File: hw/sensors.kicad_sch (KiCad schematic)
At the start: 29 parts, among them J201 BNC, U401 OPA990, U402 INA210, U403 OPA990, U404 INA210

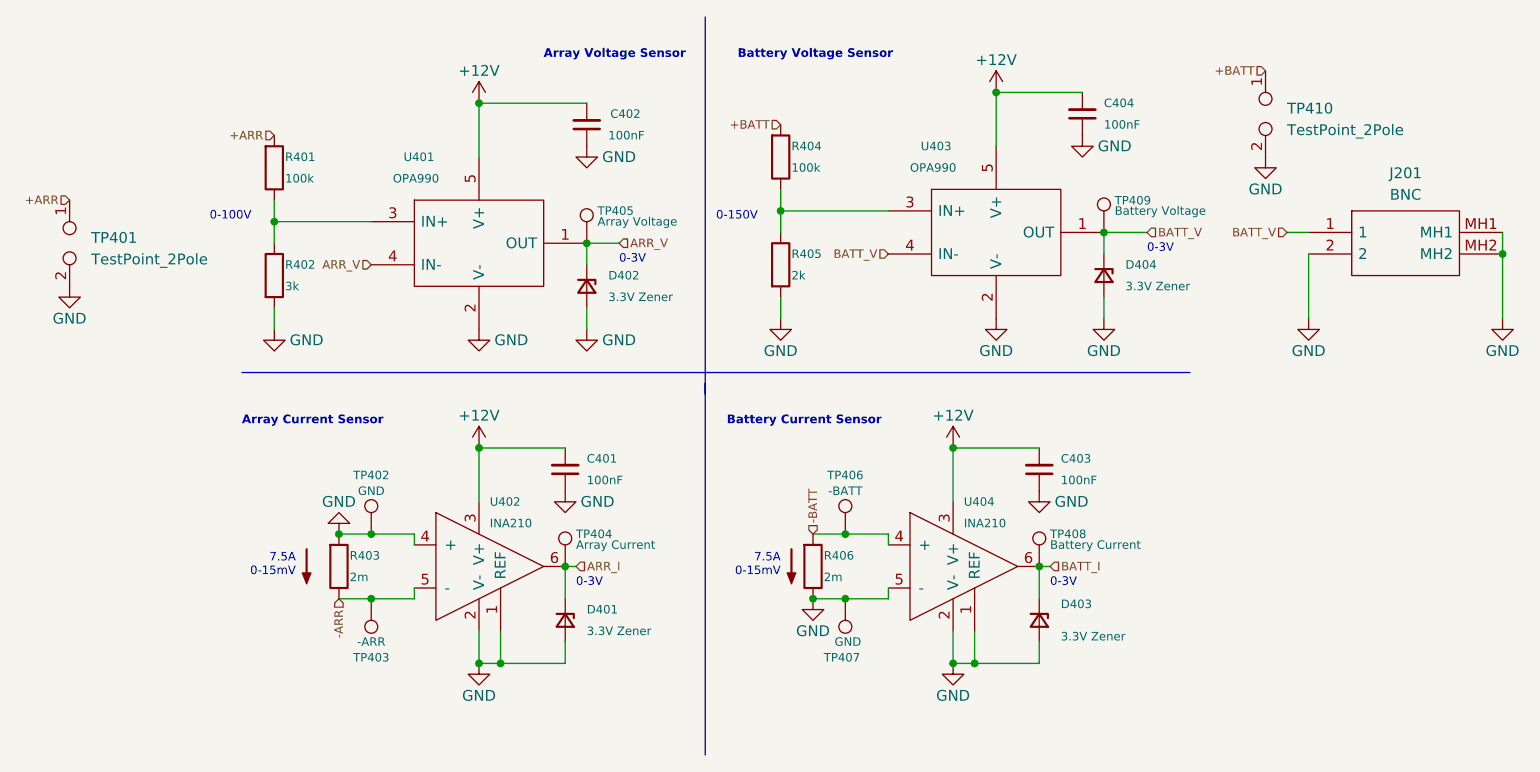
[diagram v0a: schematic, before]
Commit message: production files for v0.1.0. Change cap power calc to be based off i_rms of i_pkpk, not i_pk + r_l_a
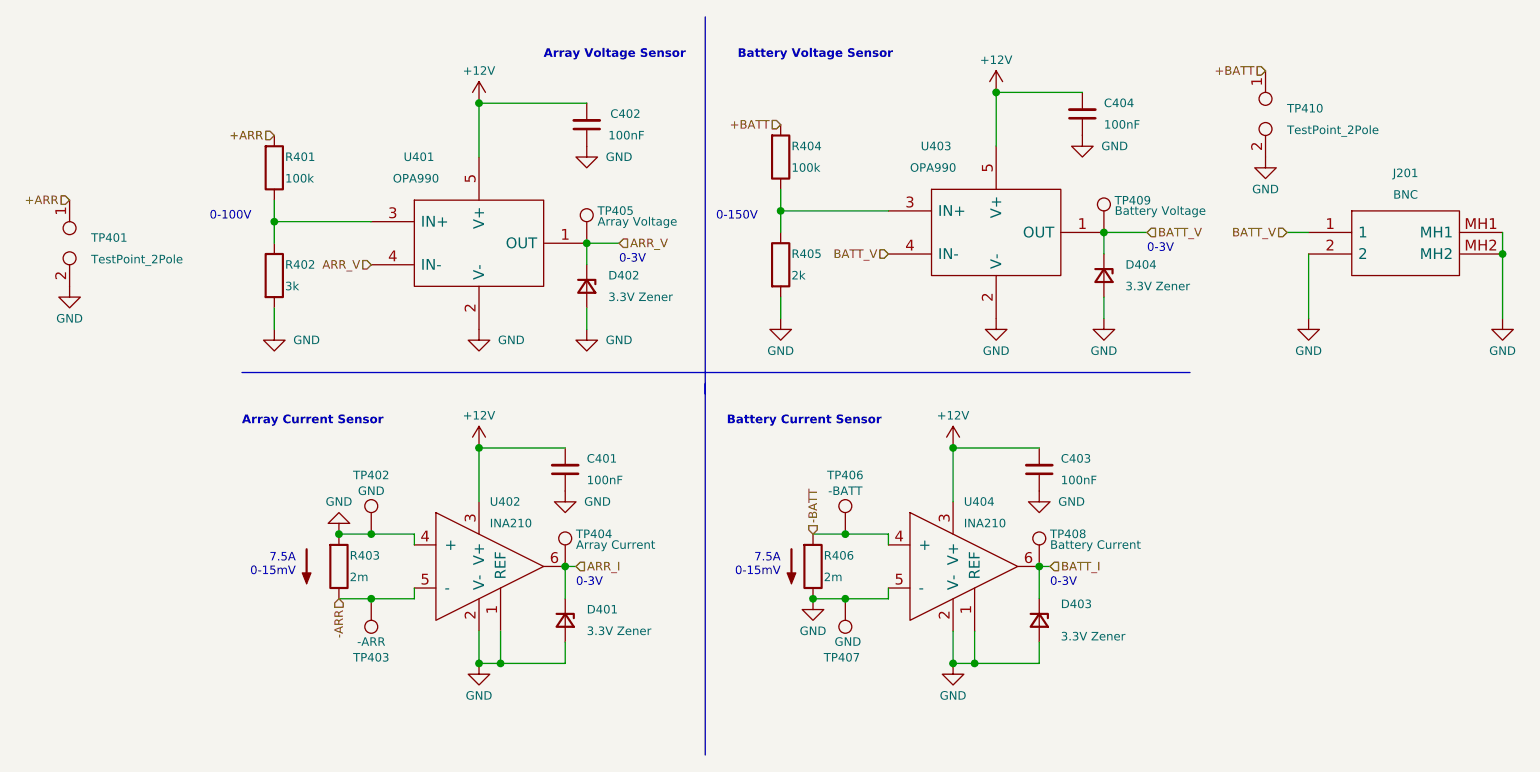
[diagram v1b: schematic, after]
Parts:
- C401, C402, C403, C404: LCSC Part # (none) -> C307331
- D401, D402, D403, D404: LCSC Part # (none) -> C8056
- R401, R404: LCSC Part # (none) -> C149504
- R402: LCSC Part # (none) -> C17661
- R405: LCSC Part # (none) -> C17604
- U402, U404: Distributor Texas Instruments -> Mouser

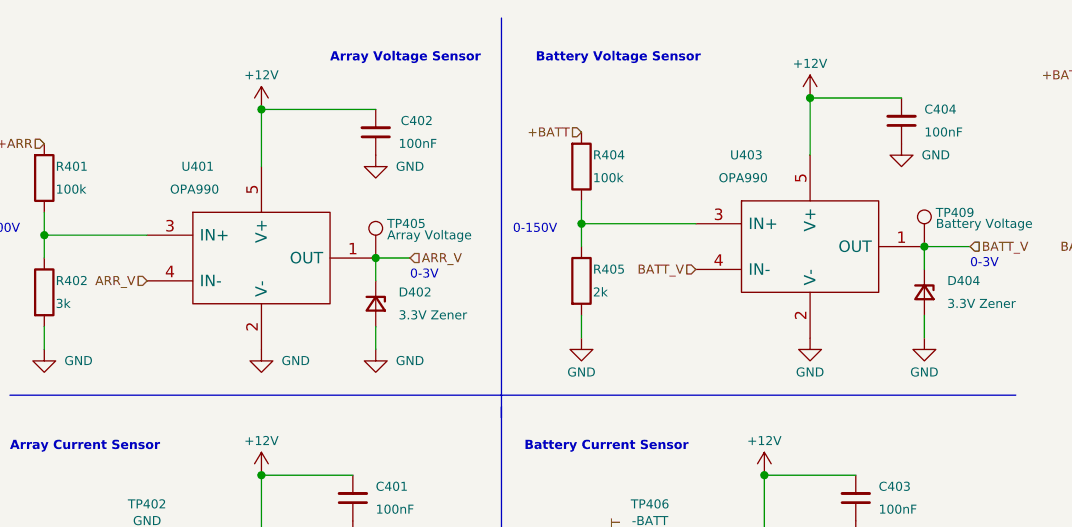
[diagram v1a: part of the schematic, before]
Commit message: fixes for v0.1.1rc
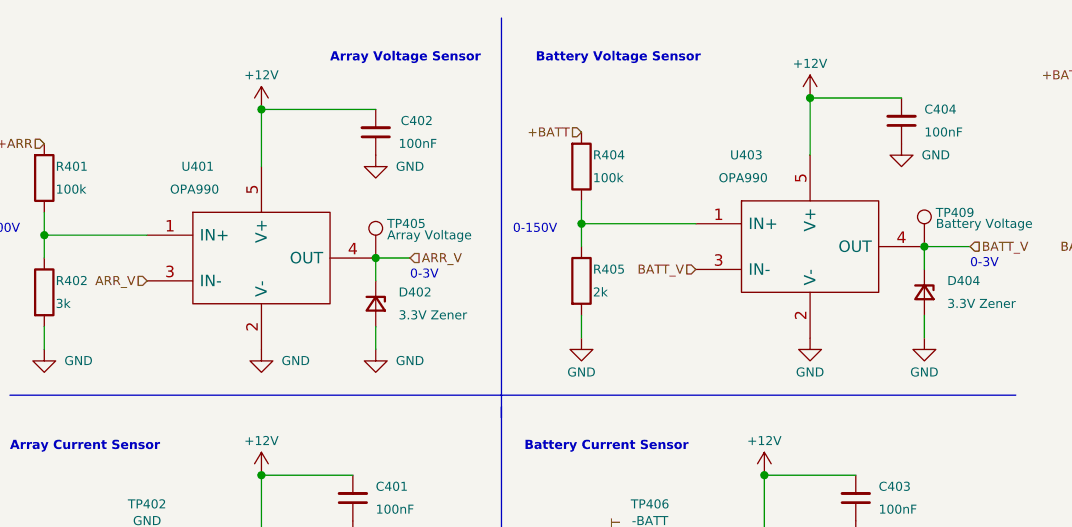
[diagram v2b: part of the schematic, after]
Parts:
- U401, U403: footprint mppt:SOT65P210X110-5N -> SOT65P210X110-5N; Height (none) -> 1.1; Manufacturer_Name (none) -> Texas Instruments; Manufacturer_Part_Number (none) -> OPA990IDCKR; Mouser Part Number (none) -> 595-OPA990IDCKR; Mouser Price/Stock (none) -> https://www.mouser.co.uk/ProductDetail/Texas-Instruments/OP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
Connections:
- net ARR_V: now also U401.3 (IN-); no longer U401.1 (OUT)
- net BATT_V: now also U403.3 (IN-); no longer U403.1 (OUT)
- net at R401.1, R402.1: now also U401.1 (IN+); no longer U401.3 (IN+)
- net at R404.1, R405.1: now also U403.1 (IN+); no longer U403.3 (IN+)
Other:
- company: (none) -> UT LHR Solar
- title: MPPT -> Sunscatter MPPT
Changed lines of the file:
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@@
   (paper "A4")
   (title_block
-    (title "MPPT")
-    (date "2023-01-30")
-    (rev "v0.0.0")
-    (comment 1 "Nishant Gupta")
+    (title "Sunscatter MPPT")
+    (date "2023-03-26")
+    (rev "v0.1.1")
+    (company "UT LHR Solar")
+    (comment 1 "Matthew Yu")
     (comment 2 "Jacob Pustilnik")
   )
@@
       (effects (font (size 1 1)) (justify left))
     )
-    (property "Footprint" "mppt:SOT65P210X110-5N" (at 190.5 71.12 0)
+    (property "Footprint" "SOT65P210X110-5N" (at 190.5 71.12 0)
       (effects (font (size 1.27 1.27)) (justify left) hide)
     )
@@
       (effects (font (size 1.27 1.27)) hide)
     )
-    (pin "1")
+    (property "Description" "Texas Instruments" (at 190.5 76.2 0)
+      (effects (font (size 1.27 1.27)) (justify left) hide)
+    )
+    (property "Height" "1.1" (at 190.5 78.74 0)
+      (effects (font (size 1.27 1.27)) (justify left) hide)
+    )
+    (property "Mouser Part Number" "595-OPA990IDCKR" (at 190.5 81.28 0)
+      (effects (font (size 1.27 1.27)) (justify left) hide)
+    )
+    (property "Mouser Price/Stock" "https://www.mouser.co.uk/ProductDetail/Texas-Instruments/OPA990IDCKR?qs=XeJtXLiO41TSF5QBGuARgQ%3D%3D" (at 190.5 83.82 0)
+      (effects (font (size 1.27 1.27)) (justify left) hide)
+    )
+    (property "Manufacturer_Name" "Texas Instruments" (at 190.5 86.36 0)
+      (effects (font (size 1.27 1.27)) (justify left) hide)
+    )
+    (property "Manufacturer_Part_Number" "OPA990IDCKR" (at 190.5 88.9 0)
+      (effects (font (size 1.27 1.27)) (justify left) hide)
+    )
     (pin "2")
+    (pin "5")
+    (pin "1")
     (pin "3")
     (pin "4")
-    (pin "5")
     (instances
       (project "mppt"
@@
       (effects (font (size 1 1)) (justify left))
     )
-    (property "Footprint" "mppt:SOT65P210X110-5N" (at 129.54 72.39 0)
+    (property "Footprint" "SOT65P210X110-5N" (at 129.54 72.39 0)
       (effects (font (size 1.27 1.27)) (justify left) hide)
     )
@@
       (effects (font (size 1.27 1.27)) hide)
     )
-    (pin "1")
+    (property "Description" "Texas Instruments" (at 129.54 77.47 0)
+      (effects (font (size 1.27 1.27)) (justify left) hide)
+    )
+    (property "Height" "1.1" (at 129.54 80.01 0)
+      (effects (font (size 1.27 1.27)) (justify left) hide)
+    )
+    (property "Mouser Part Number" "595-OPA990IDCKR" (at 129.54 82.55 0)
+      (effects (font (size 1.27 1.27)) (justify left) hide)
+    )
+    (property "Mouser Price/Stock" "https://www.mouser.co.uk/ProductDetail/Texas-Instruments/OPA990IDCKR?qs=XeJtXLiO41TSF5QBGuARgQ%3D%3D" (at 129.54 85.09 0)
+      (effects (font (size 1.27 1.27)) (justify left) hide)
+    )
+    (property "Manufacturer_Name" "Texas Instruments" (at 129.54 87.63 0)
+      (effects (font (size 1.27 1.27)) (justify left) hide)
+    )
+    (property "Manufacturer_Part_Number" "OPA990IDCKR" (at 129.54 90.17 0)
+      (effects (font (size 1.27 1.27)) (justify left) hide)
+    )
     (pin "2")
+    (pin "5")
+    (pin "1")
     (pin "3")
     (pin "4")
-    (pin "5")
-    (instances
-      (project "mppt"
+    (instances
+      (project "mppt"

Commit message: updated instructions for v0.2.0 - v0.5.0 development candidates.
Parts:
- C401, C402, C403, C404: Cost (none) -> 0.0068; JLC P/N C307331 -> (none)
- D401, D402, D403, D404: Cost (none) -> 0.0106; JLC P/N C8056 -> (none)
- J201: Cost (none) -> 2.39
- R401, R404: Cost (none) -> 0.0017; JLC P/N C149504 -> (none)
- R402: Cost (none) -> 0.0018; JLC P/N C17661 -> (none)
- R403, R406: Cost (none) -> 0.73
- R405: Cost (none) -> 0.0018; JLC P/N C17604 -> (none)
- TP402, TP407: Cost (none) -> 0.31
- TP403, TP404, TP406, TP408: Cost (none) -> 0.39
- TP405, TP409: Cost (none) -> 0.33
- U401, U403: Cost (none) -> 0.593; Distributor Mouser -> Texas Instruments; Height 1.1 -> (none); Manufacturer_Name Texas Instruments -> (none); Manufacturer_Part_Number OPA990IDCKR -> (none); Mouser Part Number 595-OPA990IDCKR -> (none); Mouser Price/Stock https://www.mouser.co.uk/ProductDetail/Texas-Instruments/OP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 -> (none); P/N 595-OPA990IDCKR -> OPA990IDCKR
- U402, U404: Cost (none) -> 0.813; Distributor Mouser -> Texas Instruments

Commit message: hw changes
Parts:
- J201: footprint mppt:CONBNC002 -> footprints:CONBNC002
- TP401, TP410: footprint mppt:SignalTP -> footprints:SignalTP
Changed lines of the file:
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@@
       (effects (font (size 1 1)) (justify left))
     )
-    (property "Footprint" "mppt:SignalTP" (at 72.39 77.47 0)
+    (property "Footprint" "footprints:SignalTP" (at 72.39 77.47 0)
       (effects (font (size 1.27 1.27)) hide)
     )
@@
       (effects (font (size 1 1)))
     )
-    (property "Footprint" "mppt:CONBNC002" (at 237.49 73.66 0)
+    (property "Footprint" "footprints:CONBNC002" (at 237.49 73.66 0)
       (effects (font (size 1.27 1.27)) (justify left) hide)
     )
@@
       (effects (font (size 1 1)) (justify left))
     )
-    (property "Footprint" "mppt:SignalTP" (at 213.36 62.23 0)
-      (effects (font (size 1.27 1.27)) hide)
-    )
+    (property "Footprint" "footprints:SignalTP" (at 213.36 62.23 0)
+      (effects (font (size 1.27 1.27)) hide)
+    )

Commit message: v0.2.0
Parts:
- removed J201: BNC, footprints:CONBNC002, symbol CONBNC002:CONBNC002
- removed TP401, TP410: TestPoint_2Pole, footprints:SignalTP, symbol Connector:TestPoint_2Pole
- removed U401, U403: OPA990, SOT65P210X110-5N, symbol OPA990IDCKR:OPA990IDCKR
- removed U402, U404: INA210, Package_TO_SOT_SMD:SOT-363_SC-70-6_Handsoldering, symbol MPPT:OP_AMP_INA21x
- added IC401, IC404: INA210CQDCKRQ1, footprints:ti_INA210CQDCKRQ1, symbol ti_INA210CQDCKRQ1:INA210CQDCKRQ1
- added IC402, IC403: OPA990IDCKR, footprints:ti_OPA990IDCKR, symbol ti_OPA990IDCKR:OPA990IDCKR
- added TP401: +ARR_TP, TestPoint:TestPoint_Pad_1.0x1.0mm, symbol Connector:TestPoint
- added TP410: GND_TP, TestPoint:TestPoint_Pad_1.0x1.0mm, symbol Connector:TestPoint
- added TP411: BATTV_TP, TestPoint:TestPoint_Pad_1.0x1.0mm, symbol Connector:TestPoint
- added TP412: BATTI_TP, TestPoint:TestPoint_Pad_1.0x1.0mm, symbol Connector:TestPoint
- D402, D403: value 3.3V Zener -> 3V3
- TP402: value GND -> GND_TP; footprint TestPoint:TestPoint_Keystone_5000-5004_Miniature -> TestPoint:TestPoint_Pad_1.0x1.0mm; Color Black -> (none); Cost 0.31 -> (none); Distributor Mouser -> (none); Manufacturer Keystone Electronics -> (none); P/N 534-5001 -> (none)
- TP403: value -ARR -> GND_TP; footprint TestPoint:TestPoint_Keystone_5000-5004_Miniature -> TestPoint:TestPoint_Pad_1.0x1.0mm; Color Brown -> (none); Cost 0.39 -> (none); Distributor Mouser -> (none); Manufacturer Keystone Electronics -> (none); P/N 534-5115 -> (none)
- TP404: value Array Current -> -ARR_TP; footprint TestPoint:TestPoint_Keystone_5000-5004_Miniature -> TestPoint:TestPoint_Pad_1.0x1.0mm; Color Blue -> (none); Cost 0.39 -> (none); Distributor Mouser -> (none); Manufacturer Keystone Electronics -> (none); P/N 534-5117 -> (none)
- TP405: value Array Voltage -> ARRI_TP; footprint TestPoint:TestPoint_Keystone_5000-5004_Miniature -> TestPoint:TestPoint_Pad_1.0x1.0mm; Color Green -> (none); Cost 0.33 -> (none); Distributor Mouser -> (none); Manufacturer Keystone Electronics -> (none); P/N 534-5116 -> (none)
- TP406: value -BATT -> ARRV_TP; footprint TestPoint:TestPoint_Keystone_5000-5004_Miniature -> TestPoint:TestPoint_Pad_1.0x1.0mm; Color Brown -> (none); Cost 0.39 -> (none); Distributor Mouser -> (none); Manufacturer Keystone Electronics -> (none); P/N 534-5115 -> (none)
- TP407: value GND -> +BATT_TP; footprint TestPoint:TestPoint_Keystone_5000-5004_Miniature -> TestPoint:TestPoint_Pad_1.0x1.0mm; Color Black -> (none); Cost 0.31 -> (none); Distributor Mouser -> (none); Manufacturer Keystone Electronics -> (none); P/N 534-5001 -> (none)
- TP408: value Battery Current -> GND_TP; footprint TestPoint:TestPoint_Keystone_5000-5004_Miniature -> TestPoint:TestPoint_Pad_1.0x1.0mm; Color Blue -> (none); Cost 0.39 -> (none); Distributor Mouser -> (none); Manufacturer Keystone Electronics -> (none); P/N 534-5117 -> (none)
- TP409: value Battery Voltage -> -BATT_TP; footprint TestPoint:TestPoint_Keystone_5000-5004_Miniature -> TestPoint:TestPoint_Pad_1.0x1.0mm; Color Green -> (none); Cost 0.33 -> (none); Distributor Mouser -> (none); Manufacturer Keystone Electronics -> (none); P/N 534-5116 -> (none)
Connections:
- net +ARR: now also TP401.1
- net +BATT: now also TP407.1
- net -ARR: now also TP404.1, IC401.5 (IN-); no longer TP403.1
- net -BATT: now also TP409.1, IC404.4 (IN+); no longer TP406.1
- net ARR_I: now also TP405.1, IC401.6 (OUT); no longer TP404.1
- net ARR_V: now also TP406.1, IC402.3 (IN-), IC402.4 (OUT); no longer TP405.1
- net BATT_I: now also D404.1 (K), IC404.6 (OUT), TP412.1; no longer D403.1 (K), TP408.1
- net BATT_V: now also D403.1 (K), IC403.3 (IN-), IC403.4 (OUT), TP411.1; no longer D404.1 (K), TP409.1
- net GND: now also TP403.1, TP408.1, IC401.1 (REF), IC401.2 (GND), IC401.4 (IN+), IC402.2 (V-), IC403.2 (V-), IC404.1 (REF), IC404.2 (GND), IC404.5 (IN-), TP410.1; no longer TP407.1
- net at R401.1, R402.1: now also IC402.1 (IN+)
- net at R404.1, R405.1: now also IC403.1 (IN+)
- net +12V renamed +5V
- net +5V: now also IC401.3 (V+), IC402.5 (V+), IC403.5 (V+), IC404.3 (V+)
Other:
- note added: "0-113V"
- note added: "0-168V"
- note added: "0-3.3V"
- note added: "8.25A 0-16.5mV"
- note removed: "0-100V"
- note removed: "0-150V"
- note removed: "0-3V"
- note removed: "7.5A 0-15mV"
- company: UT LHR Solar -> LHR Solar
